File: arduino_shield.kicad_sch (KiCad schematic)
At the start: 7 parts

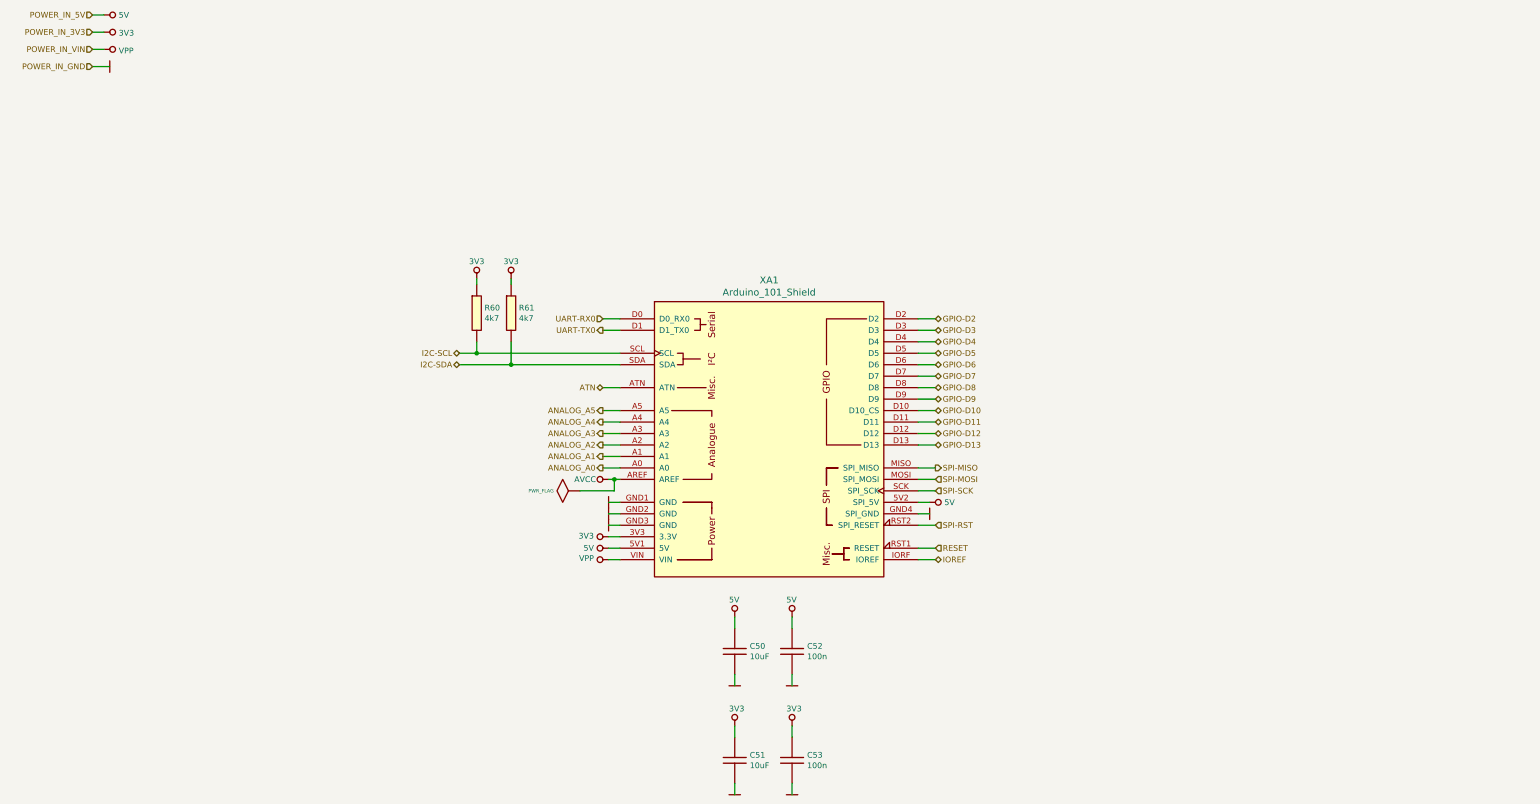
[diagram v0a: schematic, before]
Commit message: Corrected schematic
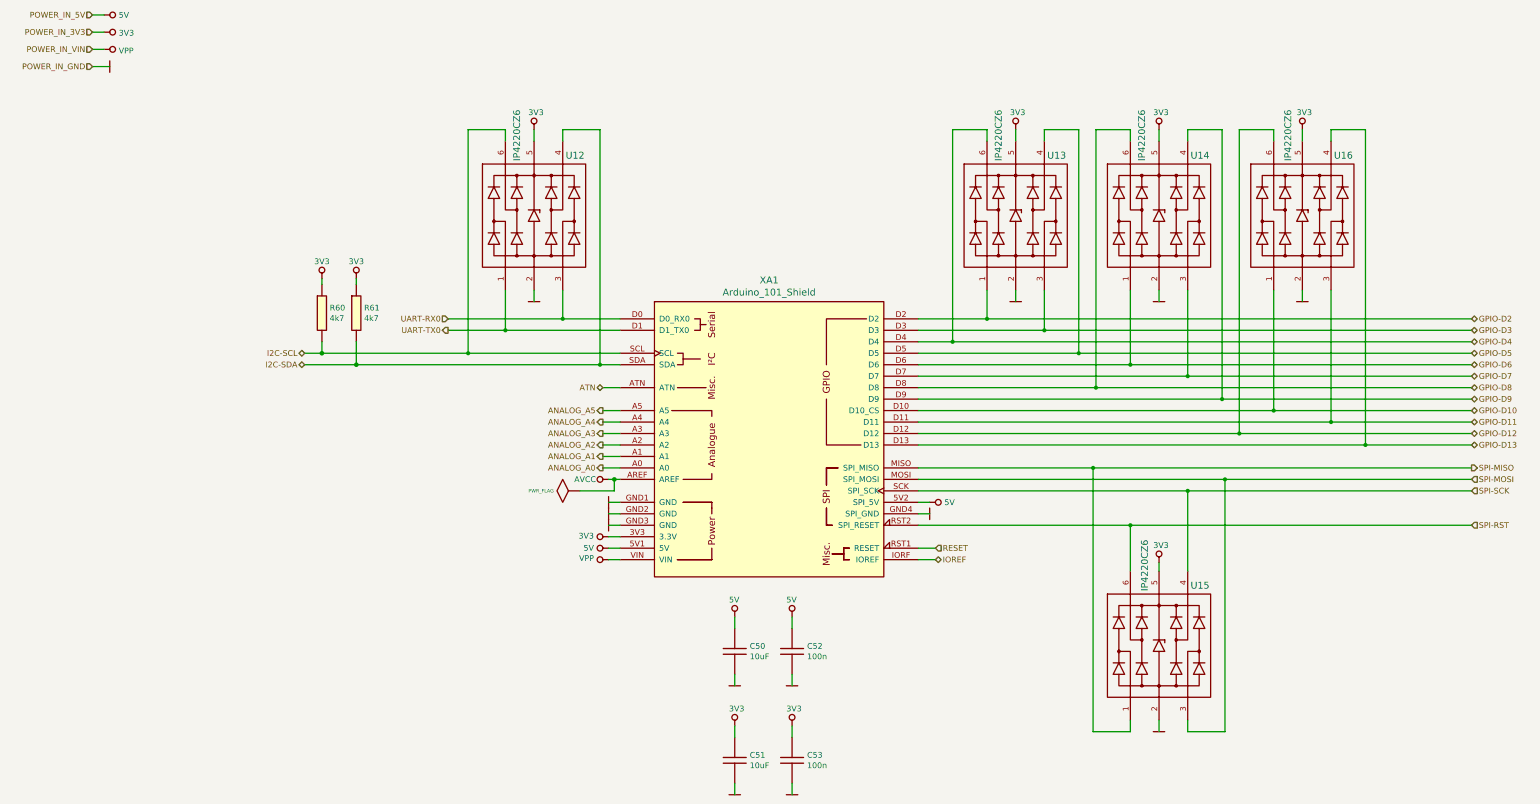
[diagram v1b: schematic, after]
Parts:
- added U12, U13, U14, U15, U16: IP4220CZ6, ESD_Protectors:IP4220CZ6_SOT457, symbol esd_protectors:IP4220CZ6
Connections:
- net 3V3: now also U12.5 (Vp), U13.5 (Vp), U14.5 (Vp), U15.5 (Vp), U16.5 (Vp)
- net GND: now also U12.2 (GND), U13.2 (GND), U14.2 (GND), U15.2 (GND), U16.2 (GND)
- net GPIO-D10: now also U16.1 (I/O1)
- net GPIO-D11: now also U16.3 (I/O2)
- net GPIO-D12: now also U16.6 (I/O4)
- net GPIO-D13: now also U16.4 (I/O3)
- net GPIO-D2: now also U13.1 (I/O1)
- net GPIO-D3: now also U13.3 (I/O2)
- net GPIO-D4: now also U13.6 (I/O4)
- net GPIO-D5: now also U13.4 (I/O3)
- net GPIO-D6: now also U14.1 (I/O1)
- net GPIO-D7: now also U14.3 (I/O2)
- net GPIO-D8: now also U14.6 (I/O4)
- net GPIO-D9: now also U14.4 (I/O3)
- net I2C-SCL: now also U12.6 (I/O4)
- net I2C-SDA: now also U12.4 (I/O3)
- net SPI-MISO: now also U15.1 (I/O1)
- net SPI-MOSI: now also U15.3 (I/O2)
- net SPI-RST: now also U15.6 (I/O4)
- net SPI-SCK: now also U15.4 (I/O3)
- net UART-RX0: now also U12.3 (I/O2)
- net UART-TX0: now also U12.1 (I/O1)
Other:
- moved on the sheet: R60, R61

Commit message: Tracking in progress
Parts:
- added U19: IP4220CZ6, ESD_Protectors:IP4220CZ6_SOT457, symbol esd_protectors:IP4220CZ6
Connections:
- net 3V3: now also U19.5 (Vp)
- net GND: now also U19.2 (GND)
- net UART-RX0: now also U19.1 (I/O1); no longer U12.3 (I/O2)
- net UART-TX0: now also U19.3 (I/O2); no longer U12.1 (I/O1)
- no-connect marks 0 -> 4
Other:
- moved on the sheet: R60, R61

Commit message: Eliminated all warnings realted with footprints
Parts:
- C52, C53: footprint Capacitors_Smd_0603:100nF_0603 -> Capacitors_Smd_0402:100nF_0402; symbol Capacitors_Smd0603:100n -> Capacitors_Smd0402:100nF; Developer (none) -> MW; LCSC Part # (optional) (none) -> C131394; Manufacturer SAMSUNG -> Murata; Manufacturer Part Number CL10B104JB8NNNC -> GRM155R71H104KE14D; Package 0603 -> 0402; Package_1 (none) -> 0402; Price@1000pcs 0,02231 -> 0,03299; Price@1pc 0,04540 -> 0,07091; Supplier TME -> Tme; Supplier Part Number CL10B104JB8NNNC -> GRM155R71H104KE14D; URL https://www.tme.eu/pl/details/cl10b104jb8nnnc/kondensatory-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 -> https://www.tme.eu/pl/details/grm155r71h104ke14d/kondensato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
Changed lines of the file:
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@@
     (pin "2")
   )
-  (symbol (lib_id "Capacitors_Smd0603:100n") (at 212.09 187.96 0) (unit 1)
+  (symbol (lib_id "Capacitors_Smd0402:100nF") (at 212.09 187.96 0) (unit 1)
     (in_bom yes) (on_board yes)
     (property "Reference" "C52" (id 0) (at 215.4174 186.7916 0)
@@
       (effects (font (size 1.27 1.27)) (justify left))
     )
-    (property "Footprint" "Capacitors_Smd_0603:100nF_0603" (id 2) (at 212.09 187.96 0)
-      (effects (font (size 1.524 1.524)) hide)
-    )
-    (property "Datasheet" "Capacitors/Smd_0603/Components_Documentation/KEM_C1005_Y5V_SMD.pdf" (id 3) (at 212.09 187.96 0)
-      (effects (font (size 1.524 1.524)) hide)
-    )
-    (property "Manufacturer" "SAMSUNG" (id 4) (at 212.09 187.96 0)
-      (effects (font (size 1.27 1.27)) hide)
-    )
-    (property "Manufacturer Part Number" "CL10B104JB8NNNC" (id 5) (at 212.09 187.96 0)
-      (effects (font (size 1.27 1.27)) hide)
-    )
-    (property "Supplier" "TME" (id 6) (at 212.09 187.96 0)
-      (effects (font (size 1.27 1.27)) hide)
-    )
-    (property "Supplier Part Number" "CL10B104JB8NNNC" (id 7) (at 212.09 187.96 0)
-      (effects (font (size 1.27 1.27)) hide)
-    )
-    (property "URL" "https://www.tme.eu/pl/details/cl10b104jb8nnnc/kondensatory-mlcc-smd-0603/samsung/" (id 8) (at 212.09 187.96 0)
-      (effects (font (size 1.27 1.27)) hide)
-    )
-    (property "Price@1pc" "0,04540" (id 9) (at 212.09 187.96 0)
-      (effects (font (size 1.27 1.27)) hide)
-    )
-    (property "Price@1000pcs" "0,02231" (id 10) (at 212.09 187.96 0)
-      (effects (font (size 1.27 1.27)) hide)
-    )
-    (property "Package" "0603" (id 11) (at 212.09 187.96 0)
+    (property "Footprint" "Capacitors_Smd_0402:100nF_0402" (id 2) (at 212.09 187.96 0)
+      (effects (font (size 1.27 1.27)) hide)
+    )
+    (property "Datasheet" "https://www.tme.eu/Document/558f361ed82994aff5a3e7789d970dd1/GRM155R71H104KE14-01.pdf" (id 3) (at 212.09 187.96 0)
+      (effects (font (size 1.27 1.27)) hide)
+    )
+    (property "Manufacturer" "Murata" (id 4) (at 212.09 187.96 0)
+      (effects (font (size 1.27 1.27)) hide)
+    )
+    (property "Manufacturer Part Number" "GRM155R71H104KE14D" (id 5) (at 212.09 187.96 0)
+      (effects (font (size 1.27 1.27)) hide)
+    )
+    (property "Supplier" "Tme" (id 6) (at 212.09 187.96 0)
+      (effects (font (size 1.27 1.27)) hide)
+    )
+    (property "Supplier Part Number" "GRM155R71H104KE14D" (id 7) (at 212.09 187.96 0)
+      (effects (font (size 1.27 1.27)) hide)
+    )
+    (property "URL" "https://www.tme.eu/pl/details/grm155r71h104ke14d/kondensatory-mlcc-smd-0402/murata/" (id 8) (at 212.09 187.96 0)
+      (effects (font (size 1.27 1.27)) hide)
+    )
+    (property "Price@1pc" "0,07091" (id 9) (at 212.09 187.96 0)
+      (effects (font (size 1.27 1.27)) hide)
+    )
+    (property "Price@1000pcs" "0,03299" (id 10) (at 212.09 187.96 0)
+      (effects (font (size 1.27 1.27)) hide)
+    )
+    (property "Package" "0402" (id 11) (at 212.09 187.96 0)
+      (effects (font (size 1.27 1.27)) hide)
+    )
+    (property "Developer" "MW" (id 12) (at 212.09 187.96 0)
+      (effects (font (size 1.27 1.27)) hide)
+    )
+    (property "Package_1" "0402" (id 13) (at 212.09 187.96 0)
+      (effects (font (size 1.27 1.27)) hide)
+    )
+    (property "LCSC Part # (optional)" "C131394" (id 14) (at 212.09 187.96 0)
       (effects (font (size 1.27 1.27)) hide)
     )
@@
     (pin "2")
   )
-  (symbol (lib_id "Capacitors_Smd0603:100n") (at 212.09 212.09 0) (unit 1)
+  (symbol (lib_id "Capacitors_Smd0402:100nF") (at 212.09 212.09 0) (unit 1)
     (in_bom yes) (on_board yes)
     (property "Reference" "C53" (id 0) (at 215.4174 210.9216 0)
@@
       (effects (font (size 1.27 1.27)) (justify left))
     )
-    (property "Footprint" "Capacitors_Smd_0603:100nF_0603" (id 2) (at 212.09 212.09 0)
-      (effects (font (size 1.524 1.524)) hide)
-    )
-    (property "Datasheet" "Capacitors/Smd_0603/Components_Documentation/KEM_C1005_Y5V_SMD.pdf" (id 3) (at 212.09 212.09 0)
-      (effects (font (size 1.524 1.524)) hide)
-    )
-    (property "Manufacturer" "SAMSUNG" (id 4) (at 212.09 212.09 0)
-      (effects (font (size 1.27 1.27)) hide)
-    )
-    (property "Manufacturer Part Number" "CL10B104JB8NNNC" (id 5) (at 212.09 212.09 0)
-      (effects (font (size 1.27 1.27)) hide)
-    )
-    (property "Supplier" "TME" (id 6) (at 212.09 212.09 0)
-      (effects (font (size 1.27 1.27)) hide)
-    )
-    (property "Supplier Part Number" "CL10B104JB8NNNC" (id 7) (at 212.09 212.09 0)
-      (effects (font (size 1.27 1.27)) hide)
-    )
-    (property "URL" "https://www.tme.eu/pl/details/cl10b104jb8nnnc/kondensatory-mlcc-smd-0603/samsung/" (id 8) (at 212.09 212.09 0)
-      (effects (font (size 1.27 1.27)) hide)
-    )
-    (property "Price@1pc" "0,04540" (id 9) (at 212.09 212.09 0)
-      (effects (font (size 1.27 1.27)) hide)
-    )
-    (property "Price@1000pcs" "0,02231" (id 10) (at 212.09 212.09 0)
-      (effects (font (size 1.27 1.27)) hide)
-    )
-    (property "Package" "0603" (id 11) (at 212.09 212.09 0)
-      (effects (font (size 1.27 1.27)) hide)
-    )
+    (property "Footprint" "Capacitors_Smd_0402:100nF_0402" (id 2) (at 212.09 212.09 0)
+      (effects (font (size 1.27 1.27)) hide)
+    )
+    (property "Datasheet" "https://www.tme.eu/Document/558f361ed82994aff5a3e7789d970dd1/GRM155R71H104KE14-01.pdf" (id 3) (at 212.09 212.09 0)
+      (effects (font (size 1.27 1.27)) hide)
+    )
+    (property "Manufacturer" "Murata" (id 4) (at 212.09 212.09 0)
+      (effects (font (size 1.27 1.27)) hide)
+    )
+    (property "Manufacturer Part Number" "GRM155R71H104KE14D" (id 5) (at 212.09 212.09 0)
+      (effects (font (size 1.27 1.27)) hide)
+    )
+    (property "Supplier" "Tme" (id 6) (at 212.09 212.09 0)
+      (effects (font (size 1.27 1.27)) hide)
+    )
+    (property "Supplier Part Number" "GRM155R71H104KE14D" (id 7) (at 212.09 212.09 0)
+      (effects (font (size 1.27 1.27)) hide)
+    )
+    (property "URL" "https://www.tme.eu/pl/details/grm155r71h104ke14d/kondensatory-mlcc-smd-0402/murata/" (id 8) (at 212.09 212.09 0)
+      (effects (font (size 1.27 1.27)) hide)
+    )
+    (property "Price@1pc" "0,07091" (id 9) (at 212.09 212.09 0)
+      (effects (font (size 1.27 1.27)) hide)
+    )
+    (property "Price@1000pcs" "0,03299" (id 10) (at 212.09 212.09 0)
+      (effects (font (size 1.27 1.27)) hide)
+    )
+    (property "Package" "0402" (id 11) (at 212.09 212.09 0)
+      (effects (font (size 1.27 1.27)) hide)
+    )
+    (property "Developer" "MW" (id 12) (at 212.09 212.09 0)
+      (effects (font (size 1.27 1.27)) hide)
+    )
+    (property "Package_1" "0402" (id 13) (at 212.09 212.09 0)
+      (effects (font (size 1.27 1.27)) hide)
+    )
+    (property "LCSC Part # (optional)" "C131394" (id 14) (at 212.09 212.09 0)
+      (effects (font (size 1.27 1.27)) hide)
+    )

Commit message: Gerbers created, BOM, CPL
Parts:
- C52, C53: value 100n -> 100nF/50V
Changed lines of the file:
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@@
       (effects (font (size 1.27 1.27)) hide)
     )
-    (property "Datasheet" "Resistors/Smd_0603/Components_Documentation/Vishay_Resistors_SM0603.pdf" (id 3) (at 64.77 113.03 0)
+    (property "Datasheet" "https://www.tme.eu/Document/b315665a56acbc42df513c99b390ad98/ROYALOHM-THICKFILM.pdf" (id 3) (at 64.77 113.03 0)
       (effects (font (size 1.27 1.27)) hide)
     )
@@
       (effects (font (size 1.27 1.27)) hide)
     )
-    (property "Datasheet" "Resistors/Smd_0603/Components_Documentation/Vishay_Resistors_SM0603.pdf" (id 3) (at 72.39 113.03 0)
+    (property "Datasheet" "https://www.tme.eu/Document/b315665a56acbc42df513c99b390ad98/ROYALOHM-THICKFILM.pdf" (id 3) (at 72.39 113.03 0)
       (effects (font (size 1.27 1.27)) hide)
     )
@@
       (effects (font (size 1.27 1.27)) (justify left))
     )
-    (property "Value" "100n" (id 1) (at 215.4174 189.103 0)
+    (property "Value" "100nF/50V" (id 1) (at 215.4174 189.103 0)
       (effects (font (size 1.27 1.27)) (justify left))
     )
@@
       (effects (font (size 1.27 1.27)) (justify left))
     )
-    (property "Value" "100n" (id 1) (at 215.4174 213.233 0)
-      (effects (font (size 1.27 1.27)) (justify left))
-    )
+    (property "Value" "100nF/50V" (id 1) (at 215.4174 213.233 0)
+      (effects (font (size 1.27 1.27)) (justify left))
+    )
